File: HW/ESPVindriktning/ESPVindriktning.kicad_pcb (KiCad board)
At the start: 2 copper layers, 38.2 x 74.9 mm, 60 parts, among them SW101 reset, SW102 boot, T101 BSS138, T102 BSS138, X101 USB_C, X102 I2C, X105 Fan, X106 PM1006, X107 I2C, X108 I2C

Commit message: Add first layout tryout
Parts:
- added C118: 1n, Capacitor_SMD:C_0603_1608Metric, F.Cu at (117.0, 102.3)
- added R116: 100R, Resistor_SMD:R_0603_1608Metric, F.Cu at (107.8, 86.6)
- added R117: 100R, Resistor_SMD:R_0603_1608Metric, F.Cu at (111.7, 95.8)
- added REF**: MountingHole_2.2mm_M2, MountingHole:MountingHole_2.2mm_M2, F.Cu at (103.5, 52.5)
- added REF**: MountingHole_2.2mm_M2, MountingHole:MountingHole_2.2mm_M2, F.Cu at (102.5, 119.0)
- added REF**: MountingHole_2.2mm_M2, MountingHole:MountingHole_2.2mm_M2, F.Cu at (117.6, 119.0)
- C114: moved to B.Cu
- PD101: value PT26-51B/TR8 -> SFH 3716; footprint LED_SMD:LED_1210_3225Metric_Pad1.42x2.65mm_HandSolder -> LED_SMD:LED_0805_2012Metric_Pad1.15x1.40mm_HandSolder
- R115: value 1k -> 470R
- X102: value I2C -> WS2812
- moved C101 33.6 mm to (117.0, 109.8)
- moved R111 24.8 mm to (100.6, 84.0), turned to -90 degrees
- moved R110 23.6 mm to (102.1, 84.0), turned to -90 degrees
- moved C110 2.39 mm to (107.8, 58.5), turned to -90 degrees
- moved X102 1.36 mm to (110.0, 54.3)
- moved X107 1.36 mm to (117.9, 54.3)
- moved C114 1.08 mm to (117.7, 57.7)
- turned R101 to 180 degrees
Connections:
- C101 pad 1: /~{RESET} -> Net-(D101-A2)
- C103 pad 1: +3.3V -> +5V
- C104 pad 1: +3.3V -> +5V
- C107 pad 1: +3.3V -> +5V
- C110 pad 1: +3.3V -> +5V
- D101 pad 2: /~{RESET} -> Net-(D101-A2)
- D102 pad 2: /GPIO0 -> Net-(D102-A2)
- D105 pad 1: +3.3V -> +5V
- D106 pad 1: +3.3V -> +5V
- D107 pad 1: +3.3V -> +5V
- S102 pad 13: /USB_D+ -> /USB_D-
- S102 pad 14: /USB_D- -> /USB_D+
- S102 pad 17: /I2C_SDA -> /BUZZER
- S102 pad 18: /I2C_SCL -> /FAN
- S102 pad 6: /FAN -> /I2C_SCL
- S102 pad 7: /BUZZER -> /I2C_SDA
- SW101 pad 2: /~{RESET} -> Net-(D101-A2)
- SW102 pad 2: /GPIO0 -> Net-(D102-A2)
- X102 pad 1: +3.3V -> +5V
- X108 pad 3: /RXD0 -> /TXD0
- X108 pad 4: /TXD0 -> /RXD0
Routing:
- net +5V: track 69.8 -> 119.6 mm, vias 8 -> 9
- net +3.3V: track 104.9 -> 67.8 mm, vias 85 -> 82
- net Net-(D102-A2): track 0.00 -> 30.5 mm
- net /GPIO0: track 38.4 -> 8.67 mm
- net /~{RESET}: track 52.3 -> 26.7 mm
- net Net-(D101-A2): track 0.00 -> 24.7 mm
- net /BUZZER: track 10.3 -> 31.4 mm, vias 0 -> 2
- net GND: track 46.6 -> 58.5 mm, vias 63 -> 68
- net /PM_TX: track 41.4 -> 33.2 mm, vias 2 -> 0
- net /FAN: track 41.2 -> 33.0 mm, vias 1 -> 3
- net /PM_RX: track 42.7 -> 34.7 mm, vias 2 -> 0
- net /I2C_SCL: track 65.5 -> 59.1 mm
- net /TXD0: track 10.9 -> 13.9 mm
- net /WS2812_DI: track 18.9 -> 20.5 mm
- net Net-(D105-DOUT): track 12.0 -> 13.4 mm
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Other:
- outline, holes or cut-outs redrawn

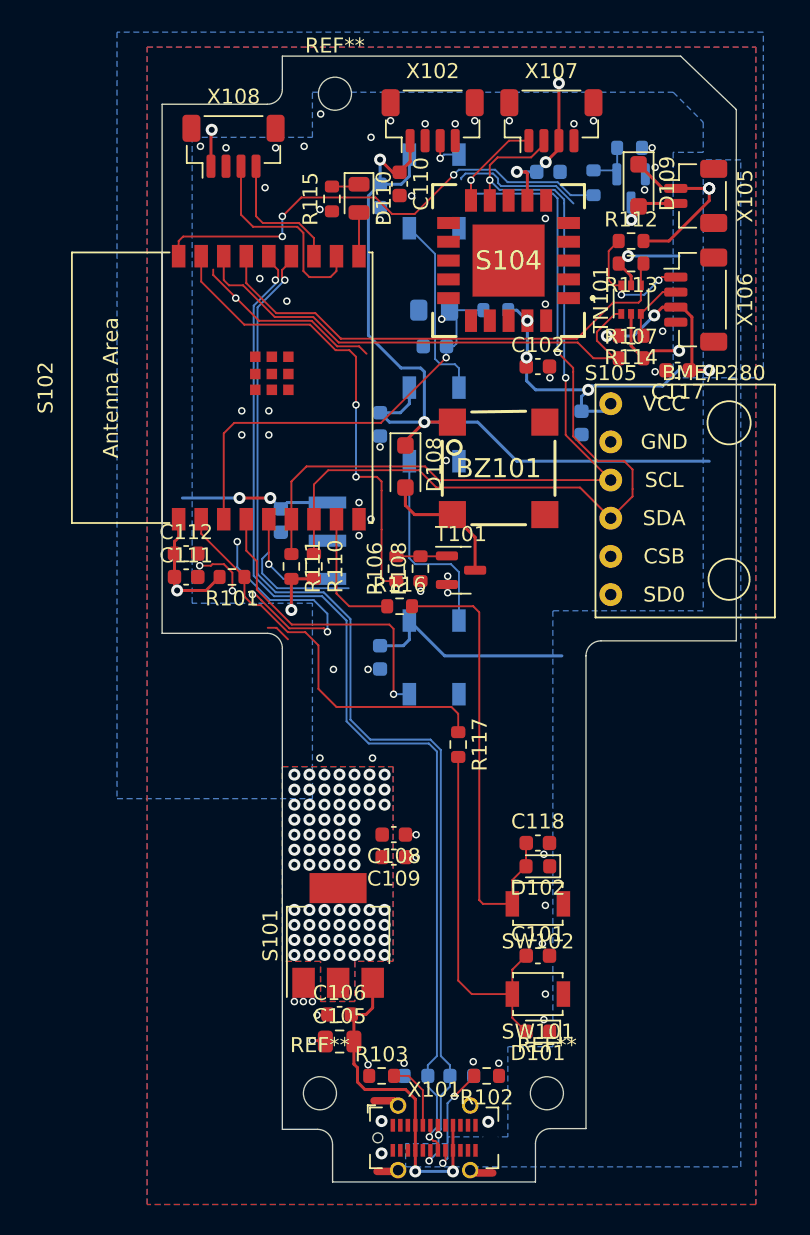
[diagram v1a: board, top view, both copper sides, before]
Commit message: Review and layout optimization
Changes to schematic:
 - Add BME280 as ASIC under the module
 - Reduce I2C Pull-Ups to 1.2k

Changes to layout:
 - Optimize parts placement
 - Make USB approx. 9ß OHm impedance
 - General routing improvements
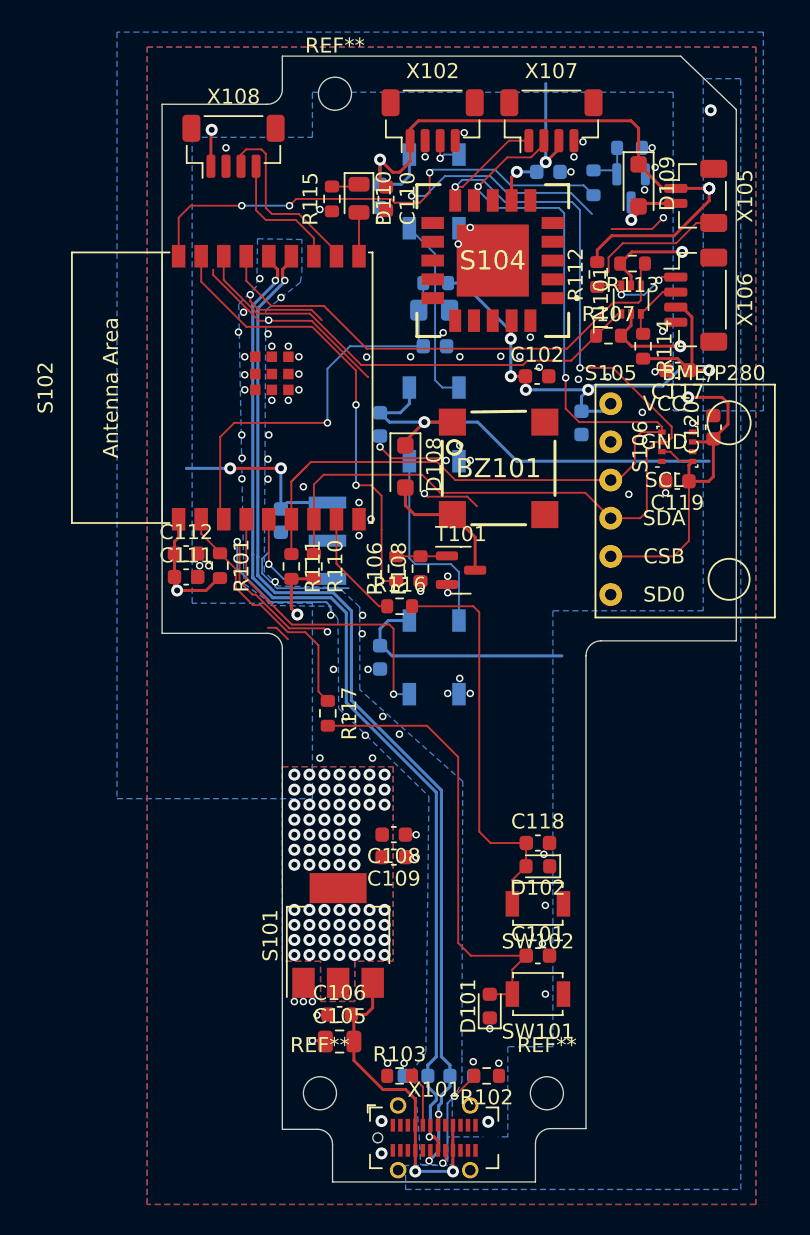
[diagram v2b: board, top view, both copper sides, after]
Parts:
- added C119: 100n, Capacitor_SMD:C_0603_1608Metric, F.Cu at (126.3, 78.3)
- added C120: 100n, Capacitor_SMD:C_0603_1608Metric, F.Cu at (128.7, 74.7)
- added S106: BME280, Package_LGA:Bosch_LGA-8_2.5x2.5mm_P0.65mm_ClockwisePinNumbering, F.Cu at (126.3, 76.0)
- R110, R111: value 4.7k -> 1.2k
- S105: value module_bme280 -> BME280
- moved R117 8.92 mm to (103.0, 93.7)
- moved R104 4.39 mm to (110.2, 65.1)
- moved D101 3.62 mm to (113.8, 113.2), turned to 90 degrees
- moved R112 3.16 mm to (121.0, 64.5), turned to 90 degrees
- moved R107 2.12 mm to (121.7, 68.6)
- moved C110 1.33 mm to (106.9, 59.5)
- moved R103 1.20 mm to (107.8, 117.8)
- moved R101 1.10 mm to (95.8, 83.9), turned to -90 degrees
- moved R114 1.06 mm to (124.0, 69.3), turned to -90 degrees
- moved S104 1.05 mm to (114.0, 63.6)
- moved C102 0.65 mm to (117.0, 71.3)
- moved R113 0.10 mm to (123.3, 63.8)
- turned C115 to 0 degrees
- turned PD101 to 0 degrees
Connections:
- net /GPIO0 renamed /BOOT
- S105 pad 5: unconnected-(S105-CSB-Pad5) -> +3.3V
- S105 pad 6: unconnected-(S105-SDO-Pad6) -> GND
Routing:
- net +3.3V: track 67.8 -> 101.2 mm, vias 82 -> 83
- net GND: track 58.5 -> 86.6 mm, vias 68 -> 104
- net /~{RESET}: track 26.7 -> 16.6 mm
- net /I2C_SCL: track 59.1 -> 68.0 mm
- net Net-(D101-A2): track 24.7 -> 31.2 mm
- net /I2C_SDA: track 64.1 -> 69.8 mm
- net +5V: track 119.6 -> 124.1 mm, vias 9 -> 8
- net Net-(D102-A2): track 30.5 -> 27.1 mm
- net /PM_RX: track 34.7 -> 31.8 mm
- net /TX: track 8.60 -> 6.38 mm
- net /USB_D-: track 72.8 -> 70.9 mm
- net /USB_D+: track 71.5 -> 69.6 mm
- net /TXD0: track 13.9 -> 12.5 mm
- net /BRIGHT_VAL: track 29.3 -> 28.1 mm, vias 2 -> 1
- net /BOOT: track 8.67 -> 7.51 mm
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
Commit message: ESP32-C3 pinout change
Change pinout due to GPIO2 needing a Pull-Up (strapping pin)
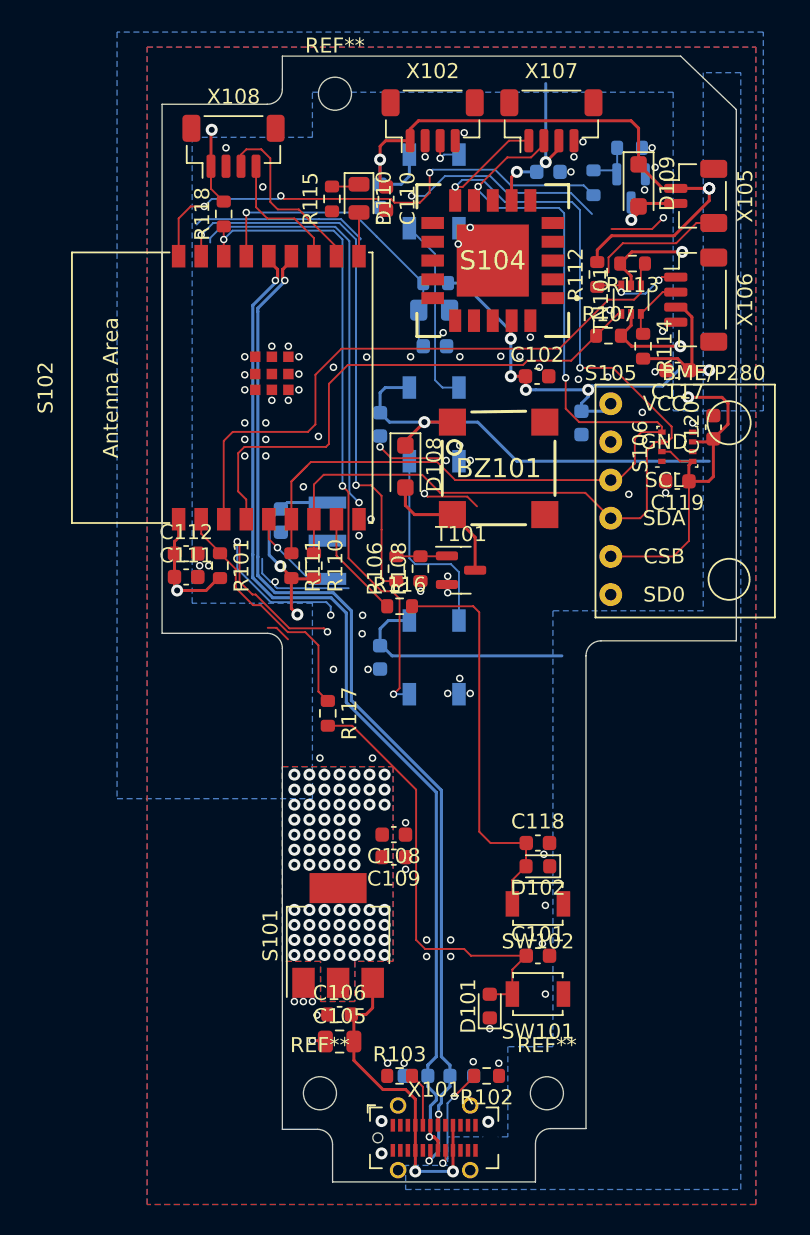
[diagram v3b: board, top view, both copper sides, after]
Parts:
- added R118: 10k, Resistor_SMD:R_0603_1608Metric, F.Cu at (96.1, 60.5)
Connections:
- S102 pad 15: /PM_TX -> /BRIGHT_VAL
- S102 pad 16: /PM_RX -> /WS2812_DI
- S102 pad 3: /BRIGHT_VAL -> /PM_TX
- S102 pad 4: /WS2812_DI -> /PM_RX
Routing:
- net /WS2812_DI: track 20.5 -> 44.0 mm, vias 1 -> 3
- net GND: track 86.6 -> 105.0 mm, vias 104 -> 100
- net /PM_TX: track 33.6 -> 41.0 mm
- net /BRIGHT_VAL: track 28.1 -> 21.1 mm
- net /BUZZER: track 30.7 -> 37.4 mm
- net /PM_RX: track 31.8 -> 36.3 mm
- net Net-(D101-A2): track 31.2 -> 29.8 mm
- net /IR_OUT: track 7.30 -> 6.32 mm
- net +5V: track 124.1 -> 123.3 mm, vias 8 -> 7
- net +3.3V: track 101.2 -> 100.4 mm, vias 83 -> 82

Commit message: Add testpoints to schematic and layout
Implement improvements from Andreas (Breaker04)
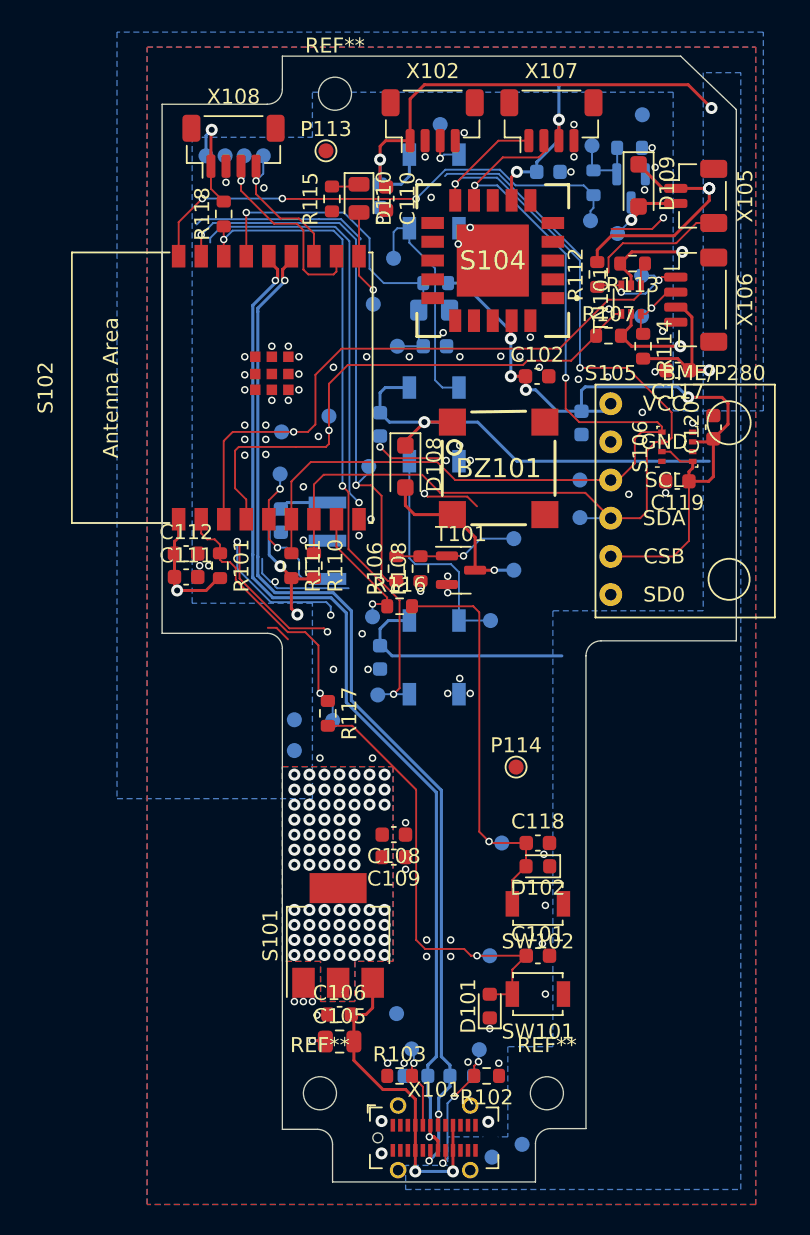
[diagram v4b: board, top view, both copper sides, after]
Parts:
- added P101: TestPoint_Small, TestPoint:TestPoint_Pad_D1.0mm, B.Cu at (113.8, 109.8)
- added P102: TestPoint_Small, TestPoint:TestPoint_Pad_D1.0mm, B.Cu at (114.6, 102.3)
- added P103: TestPoint_Small, TestPoint:TestPoint_Pad_D1.0mm, B.Cu at (113.8, 87.5)
- added P104: TestPoint_Small, TestPoint:TestPoint_Pad_D1.0mm, B.Cu at (108.6, 116.0)
- added P105: TestPoint_Small, TestPoint:TestPoint_Pad_D1.0mm, B.Cu at (113.1, 116.1)
- added P106: TestPoint_Small, TestPoint:TestPoint_Pad_D1.0mm, B.Cu at (103.3, 94.2)
- added P107: TestPoint_Small, TestPoint:TestPoint_Pad_D1.0mm, B.Cu at (107.4, 63.5)
- added P108: TestPoint_Small, TestPoint:TestPoint_Pad_D1.0mm, B.Cu at (120.5, 61.0)
- added P109: TestPoint_Small, TestPoint:TestPoint_Pad_D1.0mm, B.Cu at (105.8, 77.3)
- added P110: TestPoint_Small, TestPoint:TestPoint_Pad_D1.0mm, B.Cu at (116.0, 122.4)
- added P111: TestPoint_Small, TestPoint:TestPoint_Pad_D1.0mm, B.Cu at (107.6, 113.7)
- added P112: TestPoint_Small, TestPoint:TestPoint_Pad_D1.0mm, B.Cu at (110.5, 54.5)
- added P113: TestPoint_Small, TestPoint:TestPoint_Pad_D1.0mm, F.Cu at (102.9, 56.3)
- added P114: TestPoint_Small, TestPoint:TestPoint_Pad_D1.0mm, F.Cu at (115.5, 97.3)
- added P115: TestPoint_Small, TestPoint:TestPoint_Pad_D1.0mm, B.Cu at (124.0, 53.9)
- added P116: TestPoint_Small, TestPoint:TestPoint_Pad_D1.0mm, B.Cu at (100.8, 96.2)
- added P117: TestPoint_Small, TestPoint:TestPoint_Pad_D1.0mm, B.Cu at (100.0, 75.0)
- added P118: TestPoint_Small, TestPoint:TestPoint_Pad_D1.0mm, B.Cu at (97.5, 56.6)
- added P119: TestPoint_Small, TestPoint:TestPoint_Pad_D1.0mm, B.Cu at (98.7, 56.6)
- added P120: TestPoint_Small, TestPoint:TestPoint_Pad_D1.0mm, B.Cu at (106.3, 92.5)
- added P121: TestPoint_Small, TestPoint:TestPoint_Pad_D1.0mm, B.Cu at (107.7, 69.3)
- added P122: TestPoint_Small, TestPoint:TestPoint_Pad_D1.0mm, B.Cu at (103.1, 74.0)
- added P123: TestPoint_Small, TestPoint:TestPoint_Pad_D1.0mm, B.Cu at (99.8, 77.8)
- added P124: TestPoint_Small, TestPoint:TestPoint_Pad_D1.0mm, B.Cu at (119.8, 78.2)
- added P125: TestPoint_Small, TestPoint:TestPoint_Pad_D1.0mm, B.Cu at (119.8, 80.7)
- added P126: TestPoint_Small, TestPoint:TestPoint_Pad_D1.0mm, B.Cu at (106.0, 87.3)
- added P127: TestPoint_Small, TestPoint:TestPoint_Pad_D1.0mm, B.Cu at (106.0, 66.5)
- added P128: TestPoint_Small, TestPoint:TestPoint_Pad_D1.0mm, B.Cu at (123.9, 64.6)
- added P129: TestPoint_Small, TestPoint:TestPoint_Pad_D1.0mm, B.Cu at (120.6, 56.0)
- added P130: TestPoint_Small, TestPoint:TestPoint_Pad_D1.0mm, B.Cu at (122.3, 61.8)
- added P131: TestPoint_Small, TestPoint:TestPoint_Pad_D1.0mm, B.Cu at (123.9, 67.3)
- added P132: TestPoint_Small, TestPoint:TestPoint_Pad_D1.0mm, B.Cu at (115.4, 82.1)
- added P133: TestPoint_Small, TestPoint:TestPoint_Pad_D1.0mm, B.Cu at (115.4, 84.2)
- added P134: TestPoint_Small, TestPoint:TestPoint_Pad_D1.0mm, B.Cu at (114.0, 123.2)
- added P135: TestPoint_Small, TestPoint:TestPoint_Pad_D1.0mm, B.Cu at (100.8, 94.2)
- added P136: TestPoint_Small, TestPoint:TestPoint_Pad_D1.0mm, B.Cu at (94.9, 56.6)
- added P137: TestPoint_Small, TestPoint:TestPoint_Pad_D1.0mm, B.Cu at (96.2, 56.6)
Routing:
- net +5V: track 123.3 -> 128.3 mm, vias 7 -> 8
- net Net-(T101-G): track 3.37 -> 8.30 mm, vias 0 -> 1
- net /IR_OUT: track 6.32 -> 10.2 mm, vias 1 -> 2
- net Net-(D110-A): track 2.91 -> 6.49 mm, vias 0 -> 1
- net /BRIGHT_VAL: track 21.1 -> 24.0 mm
- net Net-(D106-DOUT): track 12.6 -> 15.5 mm
- net Net-(BZ101-+): track 8.89 -> 11.5 mm, vias 0 -> 1
- net /~{RESET}: track 16.6 -> 19.0 mm, vias 0 -> 1
- net GND: track 105.0 -> 102.6 mm, vias 100 -> 101
- net /TXD0: track 12.3 -> 14.7 mm, vias 0 -> 1
- net +3.3V: track 100.4 -> 102.7 mm, vias 82 -> 81
- net Net-(D107-DOUT): track 2.53 -> 4.78 mm
- net Net-(D105-DOUT): track 13.4 -> 15.5 mm
- net Net-(X101-CC1): track 3.59 -> 5.49 mm, vias 0 -> 1
- net /BOOT: track 7.19 -> 9.08 mm, vias 0 -> 1
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
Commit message: Add GND stitching, PCB production information and clean up silkscreen and fab layers
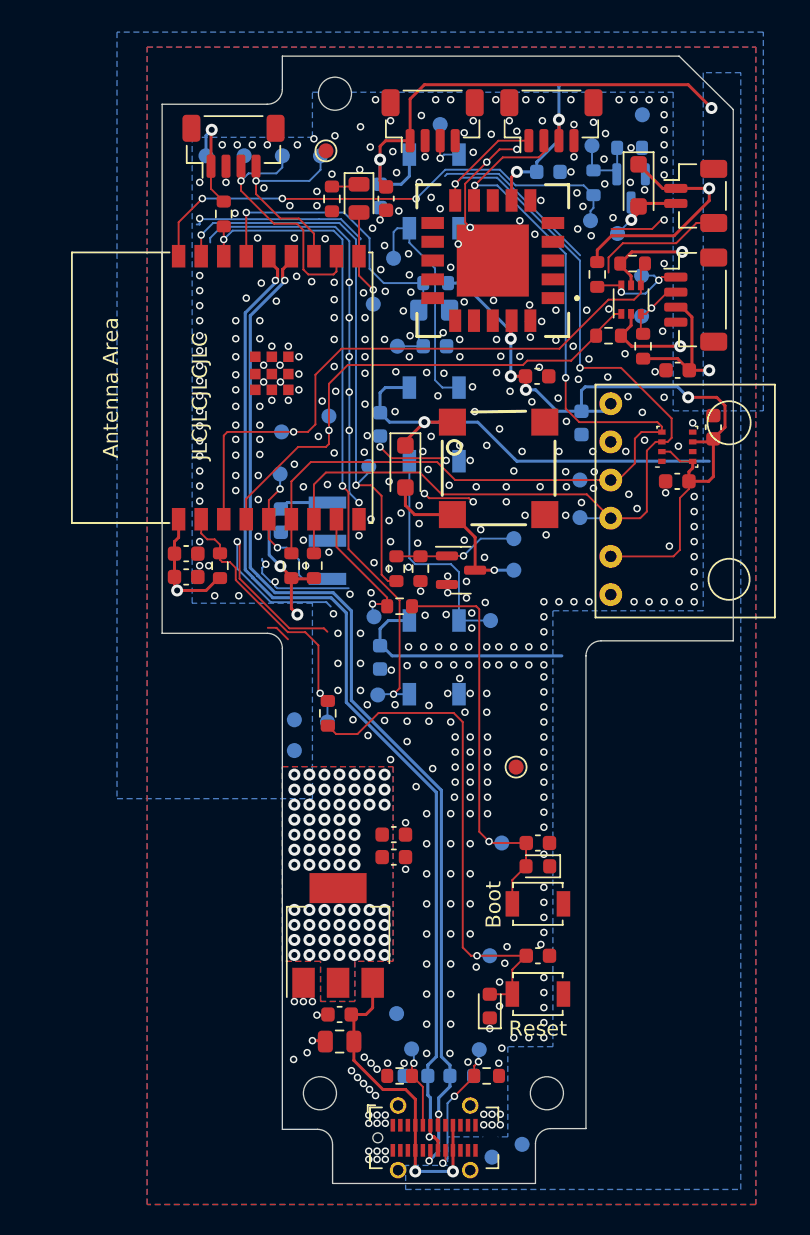
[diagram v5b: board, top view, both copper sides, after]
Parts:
- X108: value I2C -> UART
- moved P119 3.81 mm to (102.5, 56.6)
- moved P118 2.54 mm to (100.0, 56.6)
- moved P137 1.27 mm to (97.5, 56.6)
- moved P106 0.36 mm to (103.0, 94.3)
- moved P126 0.10 mm to (106.1, 87.3)
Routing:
- net GND: track 102.6 -> 109.5 mm, vias 101 -> 455
- net Net-(D101-A2): track 30.7 -> 34.8 mm
- net /RXD0: track 10.2 -> 13.8 mm
- net /PM_RX: track 37.8 -> 34.8 mm
- net /TXD0: track 14.7 -> 16.8 mm
- net +5V: vias 8 -> 7
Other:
- board size 38.2 x 74.9 mm -> 38 x 75 mm
- board text added: "0,1270 mm / 0.1270 mm"
- board text added: "0.3000 mm"
- board text added: "1.6000 mm"
- board text added: "2"
- board text added: "75.0000 mm x 38.0000 mm"
- board text added: "Castellated Pads:"
- board text added: "Copper Layers:"
- board text added: "Edge plating:"
- board text added: "Impedance controlled:"
- board text added: "JLCJLCJLCJLC"
- board text added: "Min drill dia:"
- board text added: "Min trace width/clearance:"
- board text added: "No"
- board text added: "None"
- board text added: "PCB SPECIFICATIONS"
- board text added: "PCB dimensions:"
- board text added: "PCB edge connectors:"
- board text added: "PCB thickness:"
- board text added: "Spec. copper surface:"
